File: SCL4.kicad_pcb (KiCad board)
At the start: 2 copper layers, 150.5 x 233.3 mm, 38 parts, among them J1 spare1, J2 spare2, J3 Siemens_A1010-A263, J4 SP1, J5 SP2, J6 Conn_01x08, J7 5V out, U1 MC3487DX, U2 MC3487DX, U3 TRAM Size 2, U4 MC10H125 (20PLCC), U5 MC10H124 (20PLCC)

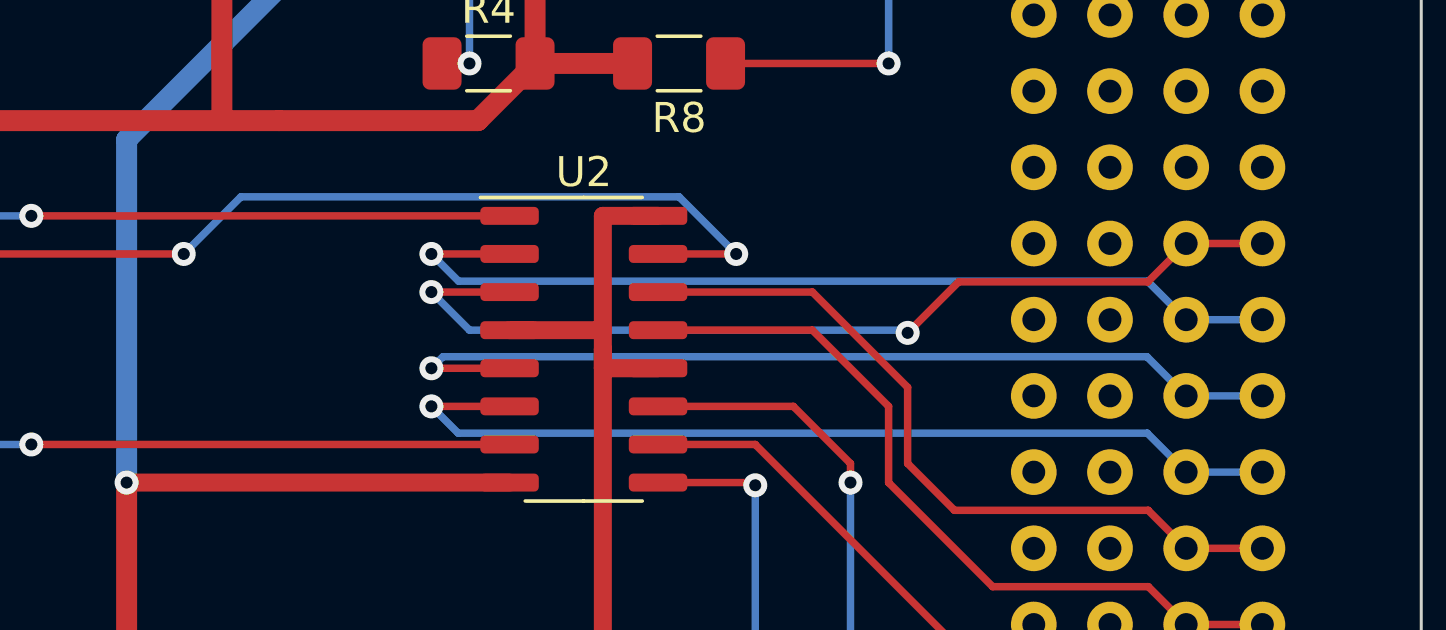
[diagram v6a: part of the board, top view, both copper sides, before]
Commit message: correct differential orientation
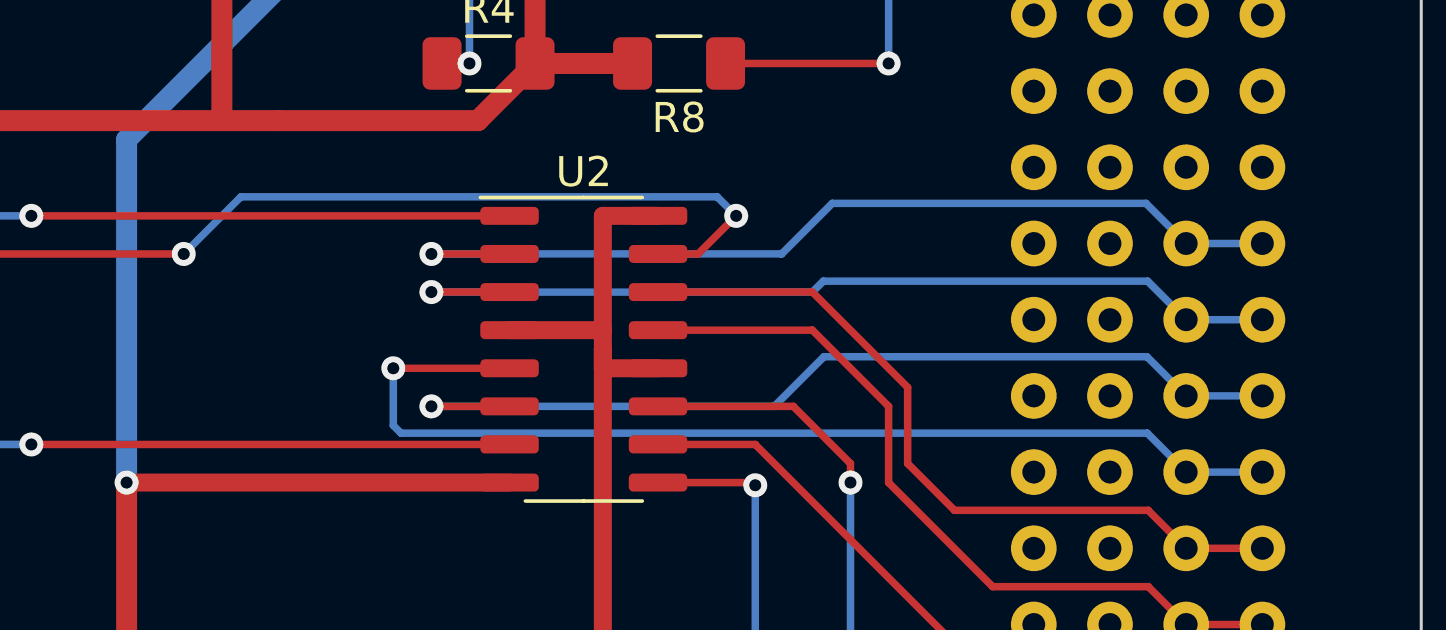
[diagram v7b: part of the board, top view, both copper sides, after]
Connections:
- J3 pad A19: //RESET -> /RESET
- J3 pad A20: /RESET -> //RESET
- J3 pad A21: //ANALYSE -> /ANALYSE
- J3 pad A22: /ANALYSE -> //ANALYSE
- J3 pad B19: //RESET -> /RESET
- J3 pad B20: /RESET -> //RESET
- J3 pad B21: //ANALYSE -> /ANALYSE
- J3 pad B22: /ANALYSE -> //ANALYSE
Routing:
- net //ANALYSE: track 31.0 -> 35.4 mm
- net //RESET: track 32.1 -> 31.0 mm, vias 2 -> 1

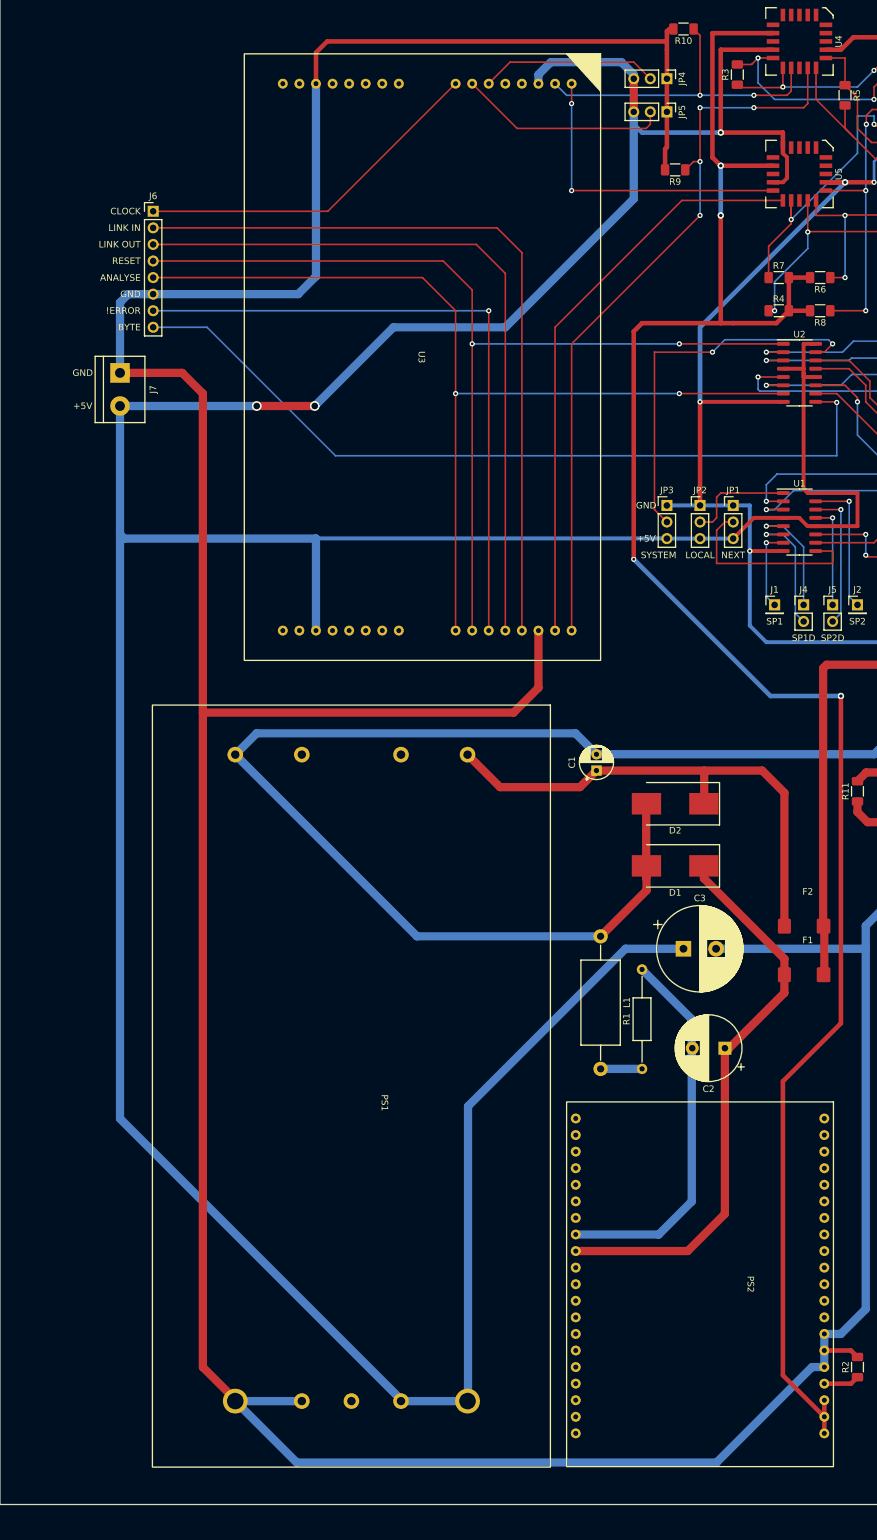
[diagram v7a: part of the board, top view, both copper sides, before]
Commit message: fixup tram pin spacing
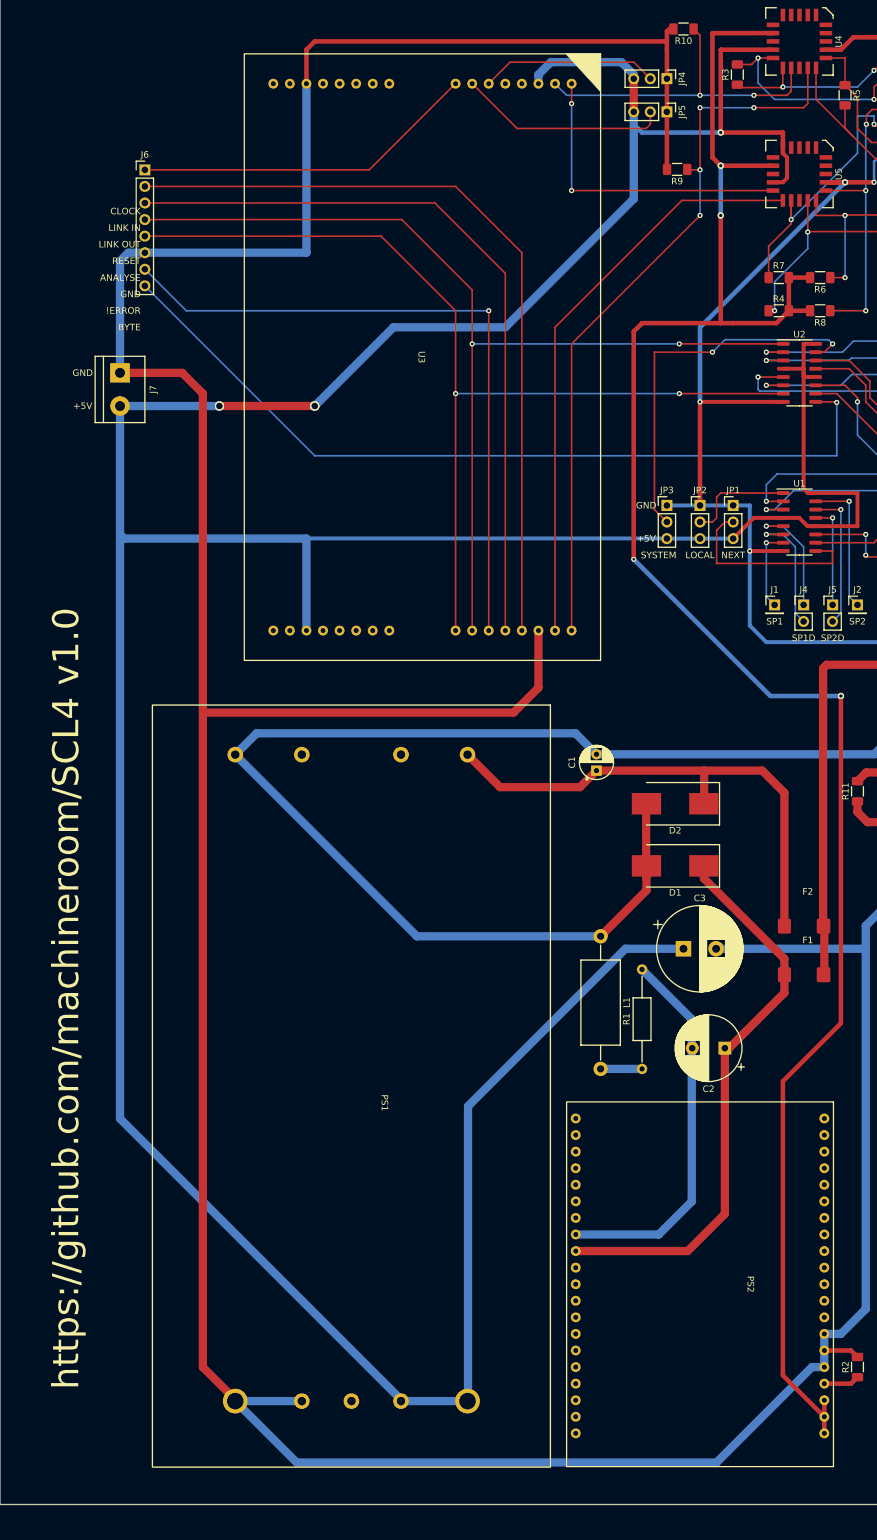
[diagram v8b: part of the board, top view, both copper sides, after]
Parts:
- moved J6 6.48 mm to (176.5, 45.1)
- moved R9 0.31 mm to (258.1, 45.0)
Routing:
- net /TL0Out: track 110.6 -> 114.5 mm
- net /TByte: track 124.4 -> 128.3 mm
- net /TReset: track 150.6 -> 154.5 mm
- net /TNotError: track 100.5 -> 104.4 mm
- net /TL0In: track 116.0 -> 119.9 mm
- net /TAnalyse: track 147.7 -> 151.6 mm
- net GND: track 910.6 -> 912.3 mm
- net /TClk: track 54.5 -> 53.1 mm
- net /TL3in: track 113.3 -> 112.8 mm
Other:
- board text added: "https://github.com/machineroom/SCL4 v1.0"
